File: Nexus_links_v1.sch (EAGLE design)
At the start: 41 parts, among them IC1 TL074D, IC4 TL074D, J1 PJ301_THONKICONN6, J10 PJ301_THONKICONN6, J11 PJ301_THONKICONN6, J12 PJ301_THONKICONN6, J2 PJ301_THONKICONN6, J3 PJ301_THONKICONN6, J4 PJ301_THONKICONN6, J5 PJ301_THONKICONN6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

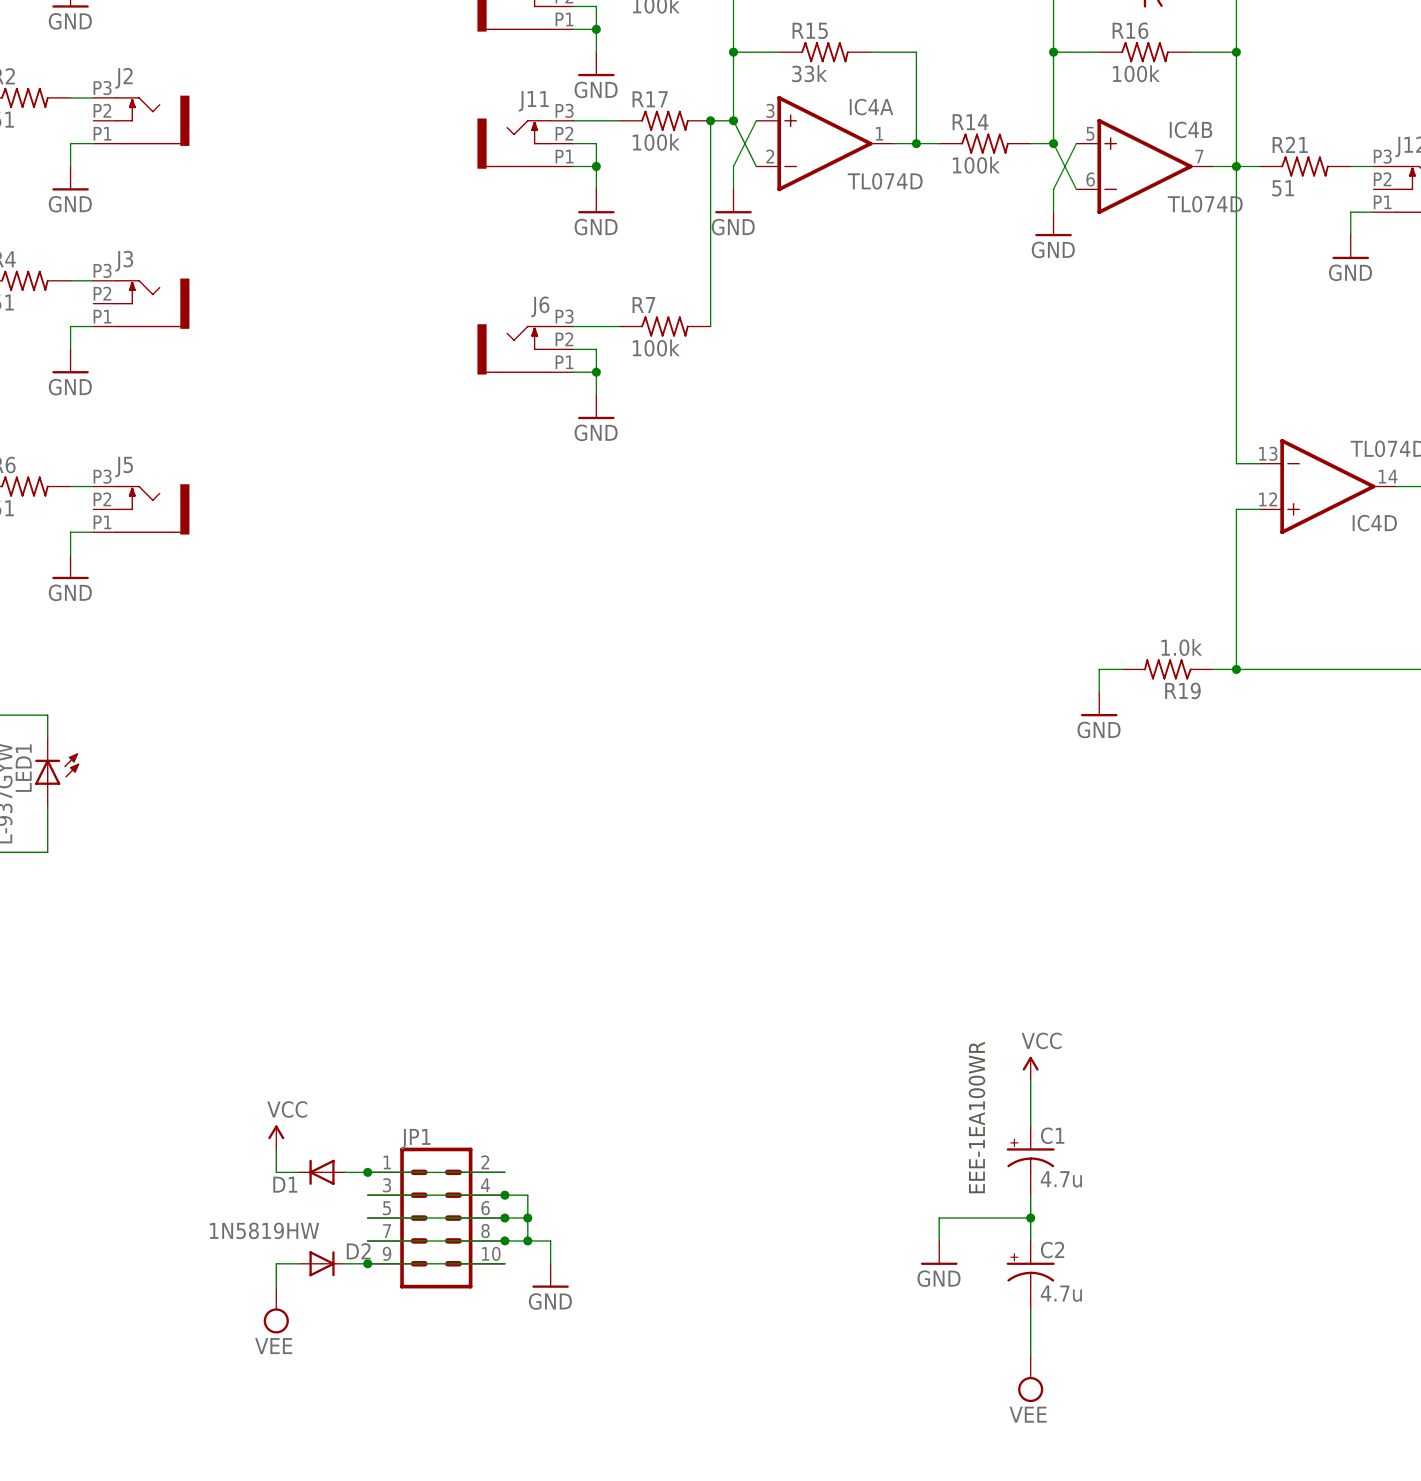
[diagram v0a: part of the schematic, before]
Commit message: Fixed power connector
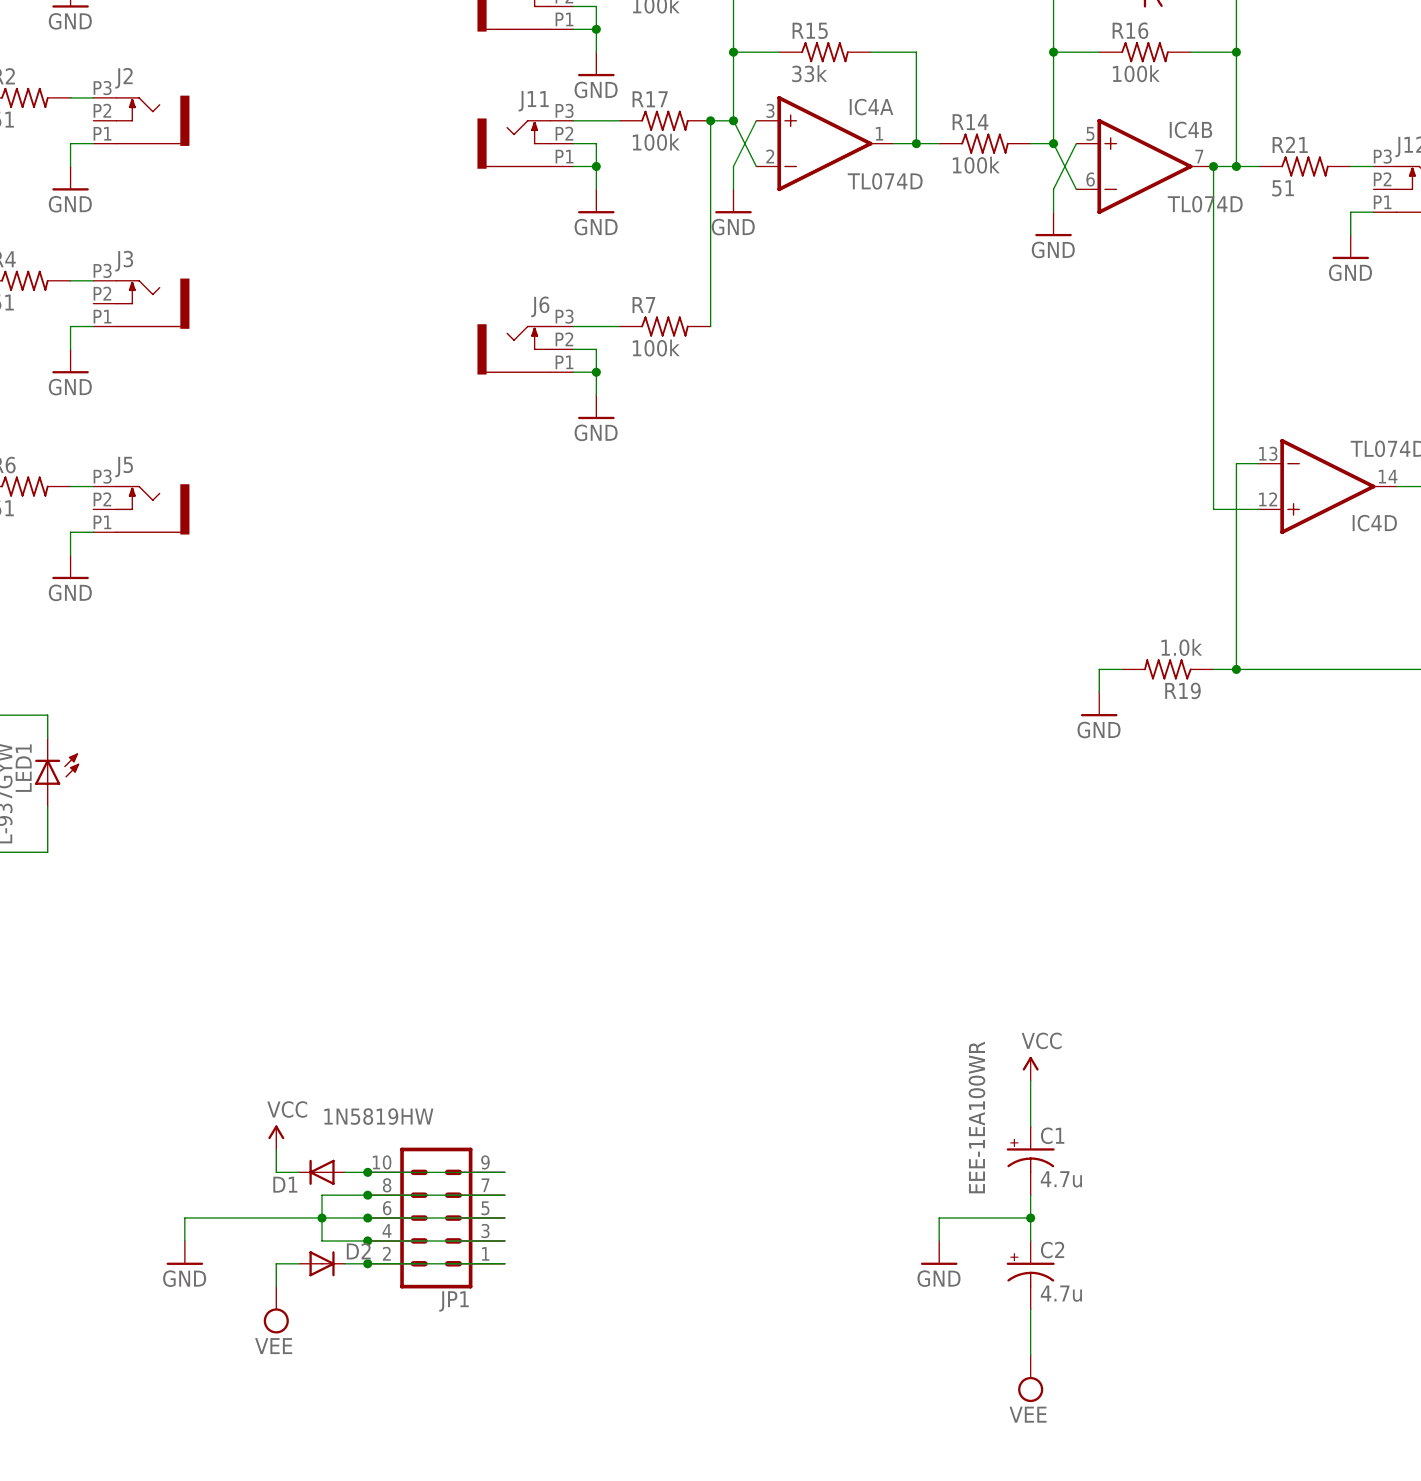
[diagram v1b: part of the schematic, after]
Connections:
- net N$18: now also IC4D.+IN; no longer IC4D.-IN
- net N$19: now also IC4D.-IN; no longer IC4D.+IN
- net N$20: now also D1.A; no longer D2.C
- net N$6: now also D2.C; no longer D1.A
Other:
- moved on the sheet: JP1
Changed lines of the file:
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@@
 <instances>
 <instance part="FRAME1" gate="G$1" x="-203.2" y="-96.52"/>
-<instance part="GND1" gate="1" x="-73.66" y="-17.78"/>
+<instance part="GND1" gate="1" x="-114.3" y="-15.24"/>
 <instance part="SUPPLY1" gate="G$1" x="-104.14" y="-20.32" rot="R180"/>
-<instance part="JP1" gate="G$1" x="-86.36" y="-10.16"/>
+<instance part="JP1" gate="G$1" x="-86.36" y="-10.16" rot="R180"/>
 <instance part="P+1" gate="1" x="-104.14" y="-2.54"/>
 <instance part="R5" gate="G$1" x="-132.08" y="134.62"/>
@@
 <instance part="D2" gate="G$1" x="-99.06" y="-15.24" smashed="yes">
 <attribute name="NAME" x="-96.52" y="-14.7574" size="1.778" layer="95"/>
-<attribute name="VALUE" x="-111.76" y="-12.4714" size="1.778" layer="96"/>
+<attribute name="VALUE" x="-99.06" y="0.2286" size="1.778" layer="96"/>
 </instance>
 <instance part="D1" gate="G$1" x="-99.06" y="-5.08" smashed="yes" rot="R180">
@@
 <net name="GND" class="0">
 <segment>
-<wire x1="-76.2" y1="-7.62" x2="-76.2" y2="-10.16" width="0.1524" layer="91"/>
-<wire x1="-76.2" y1="-10.16" x2="-76.2" y2="-12.7" width="0.1524" layer="91"/>
-<wire x1="-93.98" y1="-7.62" x2="-78.74" y2="-7.62" width="0.1524" layer="91"/>
-<wire x1="-78.74" y1="-7.62" x2="-76.2" y2="-7.62" width="0.1524" layer="91"/>
-<wire x1="-76.2" y1="-10.16" x2="-78.74" y2="-10.16" width="0.1524" layer="91"/>
-<wire x1="-78.74" y1="-10.16" x2="-93.98" y2="-10.16" width="0.1524" layer="91"/>
-<wire x1="-93.98" y1="-12.7" x2="-78.74" y2="-12.7" width="0.1524" layer="91"/>
-<wire x1="-78.74" y1="-12.7" x2="-76.2" y2="-12.7" width="0.1524" layer="91"/>
-<wire x1="-76.2" y1="-12.7" x2="-73.66" y2="-12.7" width="0.1524" layer="91"/>
-<wire x1="-73.66" y1="-12.7" x2="-73.66" y2="-15.24" width="0.1524" layer="91"/>
-<junction x="-76.2" y="-10.16"/>
-<junction x="-76.2" y="-12.7"/>
-<junction x="-78.74" y="-12.7"/>
-<junction x="-78.74" y="-10.16"/>
-<junction x="-78.74" y="-7.62"/>
 <pinref part="GND1" gate="1" pin="GND"/>
+<wire x1="-114.3" y1="-10.16" x2="-114.3" y2="-12.7" width="0.1524" layer="91"/>
+<pinref part="JP1" gate="G$1" pin="6"/>
+<wire x1="-93.98" y1="-10.16" x2="-78.74" y2="-10.16" width="0.1524" layer="91"/>
+<pinref part="JP1" gate="G$1" pin="5"/>
+<wire x1="-114.3" y1="-10.16" x2="-99.06" y2="-10.16" width="0.1524" layer="91"/>
+<junction x="-93.98" y="-10.16"/>
+<wire x1="-99.06" y1="-10.16" x2="-93.98" y2="-10.16" width="0.1524" layer="91"/>
+<wire x1="-99.06" y1="-10.16" x2="-99.06" y2="-7.62" width="0.1524" layer="91"/>
+<junction x="-99.06" y="-10.16"/>
 <pinref part="JP1" gate="G$1" pin="8"/>
-<pinref part="JP1" gate="G$1" pin="6"/>
+<wire x1="-78.74" y1="-7.62" x2="-93.98" y2="-7.62" width="0.1524" layer="91"/>
+<pinref part="JP1" gate="G$1" pin="7"/>
+<wire x1="-99.06" y1="-7.62" x2="-93.98" y2="-7.62" width="0.1524" layer="91"/>
+<junction x="-93.98" y="-7.62"/>
+<wire x1="-99.06" y1="-10.16" x2="-99.06" y2="-12.7" width="0.1524" layer="91"/>
+<wire x1="-78.74" y1="-12.7" x2="-93.98" y2="-12.7" width="0.1524" layer="91"/>
 <pinref part="JP1" gate="G$1" pin="4"/>
-<pinref part="JP1" gate="G$1" pin="7"/>
-<pinref part="JP1" gate="G$1" pin="5"/>
 <pinref part="JP1" gate="G$1" pin="3"/>
+<wire x1="-99.06" y1="-12.7" x2="-93.98" y2="-12.7" width="0.1524" layer="91"/>
+<junction x="-93.98" y="-12.7"/>
 </segment>
 <segment>
@@
 <net name="N$6" class="0">
 <segment>
-<wire x1="-93.98" y1="-5.08" x2="-78.74" y2="-5.08" width="0.1524" layer="91"/>
+<wire x1="-78.74" y1="-15.24" x2="-93.98" y2="-15.24" width="0.1524" layer="91"/>
+<pinref part="JP1" gate="G$1" pin="1"/>
+<pinref part="JP1" gate="G$1" pin="2"/>
+<pinref part="D2" gate="G$1" pin="C"/>
+<wire x1="-96.52" y1="-15.24" x2="-93.98" y2="-15.24" width="0.1524" layer="91"/>
+<junction x="-93.98" y="-15.24"/>
+</segment>
+</net>
+<net name="N$20" class="0">
+<segment>
+<wire x1="-78.74" y1="-5.08" x2="-93.98" y2="-5.08" width="0.1524" layer="91"/>
+<pinref part="JP1" gate="G$1" pin="9"/>
+<pinref part="JP1" gate="G$1" pin="10"/>
+<pinref part="D1" gate="G$1" pin="A"/>
 <wire x1="-96.52" y1="-5.08" x2="-93.98" y2="-5.08" width="0.1524" layer="91"/>
 <junction x="-93.98" y="-5.08"/>
-<pinref part="JP1" gate="G$1" pin="1"/>
-<pinref part="JP1" gate="G$1" pin="2"/>
-<pinref part="D1" gate="G$1" pin="A"/>
-</segment>
-</net>
-<net name="N$20" class="0">
-<segment>
-<wire x1="-93.98" y1="-15.24" x2="-78.74" y2="-15.24" width="0.1524" layer="91"/>
-<wire x1="-96.52" y1="-15.24" x2="-93.98" y2="-15.24" width="0.1524" layer="91"/>
-<junction x="-93.98" y="-15.24"/>
-<pinref part="JP1" gate="G$1" pin="9"/>
-<pinref part="JP1" gate="G$1" pin="10"/>
-<pinref part="D2" gate="G$1" pin="C"/>
 </segment>
 </net>
@@
 <wire x1="-2.54" y1="127" x2="2.54" y2="127" width="0.1524" layer="91"/>
 <wire x1="2.54" y1="127" x2="2.54" y2="119.38" width="0.1524" layer="91"/>
-<wire x1="5.08" y1="73.66" x2="2.54" y2="73.66" width="0.1524" layer="91"/>
-<wire x1="2.54" y1="73.66" x2="2.54" y2="106.68" width="0.1524" layer="91"/>
 <junction x="2.54" y="106.68"/>
 <junction x="2.54" y="119.38"/>
@@
 <pinref part="R16" gate="G$1" pin="2"/>
 <pinref part="C9" gate="G$1" pin="2"/>
-<pinref part="IC4" gate="D" pin="-IN"/>
+<wire x1="0" y1="106.68" x2="0" y2="68.58" width="0.1524" layer="91"/>
+<junction x="0" y="106.68"/>
+<pinref part="IC4" gate="D" pin="+IN"/>
+<wire x1="0" y1="68.58" x2="5.08" y2="68.58" width="0.1524" layer="91"/>
 </segment>
 </net>
@@
 <wire x1="30.48" y1="58.42" x2="30.48" y2="50.8" width="0.1524" layer="91"/>
 <wire x1="30.48" y1="50.8" x2="2.54" y2="50.8" width="0.1524" layer="91"/>
-<wire x1="2.54" y1="50.8" x2="2.54" y2="68.58" width="0.1524" layer="91"/>
-<wire x1="2.54" y1="68.58" x2="5.08" y2="68.58" width="0.1524" layer="91"/>
+<wire x1="2.54" y1="50.8" x2="2.54" y2="73.66" width="0.1524" layer="91"/>
 <wire x1="0" y1="50.8" x2="2.54" y2="50.8" width="0.1524" layer="91"/>
 <junction x="2.54" y="50.8"/>
 <pinref part="LED3" gate="G$1" pin="A"/>
 <pinref part="R19" gate="G$1" pin="1"/>
-<pinref part="IC4" gate="D" pin="+IN"/>
-</segment>
-</net>
+<pinref part="IC4" gate="D" pin="-IN"/>
+<wire x1="2.54" y1="73.66" x2="5.08" y2="73.66" width="0.1524" layer="91"/>
+</segment>
+</net>
